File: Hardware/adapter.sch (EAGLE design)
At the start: 8 parts

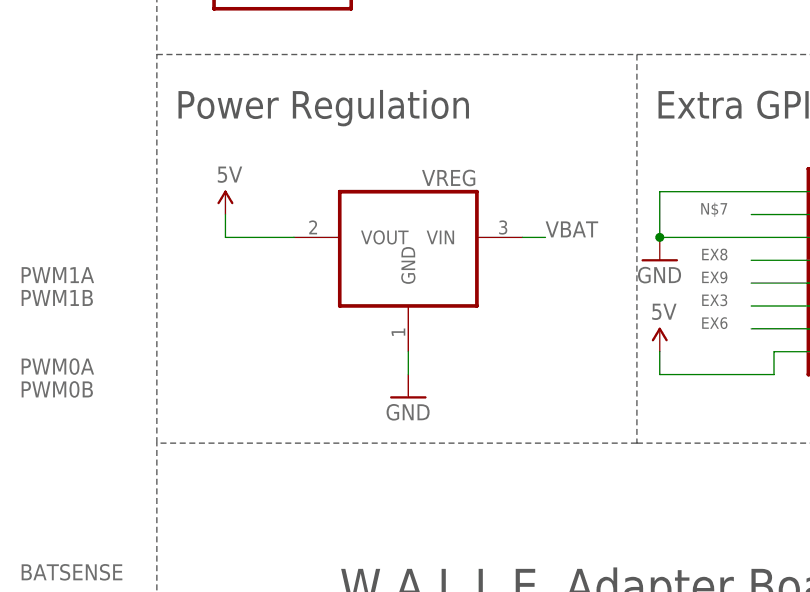
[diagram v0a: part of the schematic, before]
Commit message: Converted to TI LDO component.
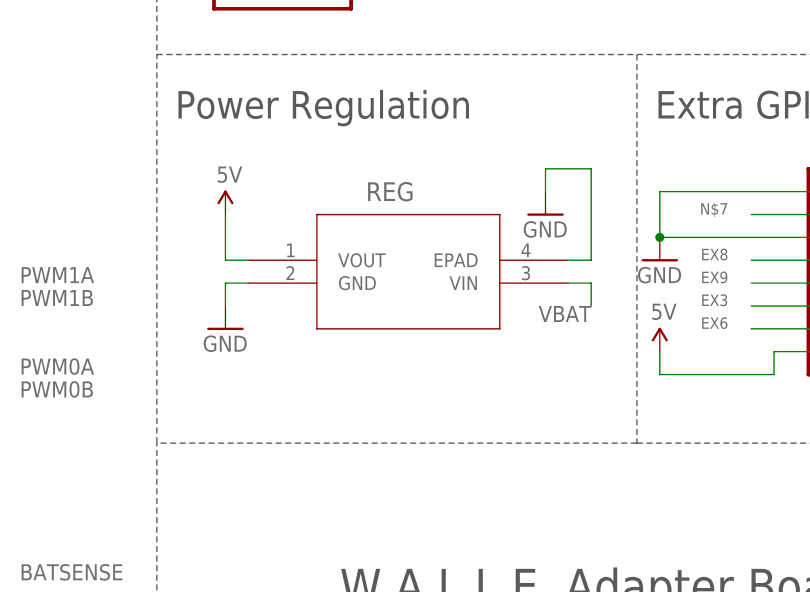
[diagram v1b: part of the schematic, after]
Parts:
- removed VREG: REG1117, burr-brown:REG1117
- added REG: UCC383-5_KTT_3, TI_UCC:UCC383-5_KTT_3
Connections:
- net 5V: now also REG.VOUT; no longer VREG.VOUT
- net GND: now also REG.EPAD, REG.GND; no longer VREG.GND
- net VBAT: now also REG.VIN; no longer VREG.VIN
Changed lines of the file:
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@@
 <part name="J1" library="pinhead" deviceset="PINHD-2X8" device=""/>
 <part name="J9" library="pinhead" deviceset="PINHD-2X8" device=""/>
-<part name="VREG" library="burr-brown" deviceset="REG1117" device=""/>
 <part name="GND9" library="supply1" deviceset="GND" device=""/>
 <part name="SUPPLY2" library="SparkFun-Aesthetics" deviceset="5V" device=""/>
@@
 <part name="GND11" library="supply1" deviceset="GND" device=""/>
 <part name="SUPPLY8" library="SparkFun-Aesthetics" deviceset="5V" device=""/>
+<part name="REG" library="TI_UCC" deviceset="UCC383-5_KTT_3" device=""/>
+<part name="GND12" library="supply1" deviceset="GND" device=""/>
 </parts>
 <sheets>
@@
 <attribute name="VALUE" x="146.05" y="93.98" size="1.778" layer="96" rot="MR180"/>
 </instance>
-<instance part="VREG" gate="G$1" x="111.76" y="38.1" smashed="yes" rot="MR0">
-<attribute name="NAME" x="119.38" y="43.815" size="1.778" layer="95" ratio="10" rot="MR0"/>
-</instance>
-<instance part="GND9" gate="1" x="111.76" y="20.32"/>
+<instance part="GND9" gate="1" x="91.44" y="27.94"/>
 <instance part="SUPPLY2" gate="G$1" x="-22.86" y="48.26"/>
 <instance part="SUPPLY3" gate="G$1" x="58.42" y="48.26"/>
@@
 <instance part="GND11" gate="1" x="177.8" y="20.32"/>
 <instance part="SUPPLY8" gate="G$1" x="139.7" y="25.4"/>
+<instance part="REG" gate="A" x="93.98" y="35.56" smashed="yes">
+<attribute name="NAME" x="107.0356" y="42.1386" size="2.0828" layer="95" ratio="6" rot="SR0"/>
+</instance>
+<instance part="GND12" gate="1" x="127" y="40.64"/>
 </instances>
 <busses>
@@
 <segment>
 <pinref part="GND9" gate="1" pin="GND"/>
-<pinref part="VREG" gate="G$1" pin="GND"/>
-<wire x1="111.76" y1="22.86" x2="111.76" y2="25.4" width="0.1524" layer="91"/>
+<wire x1="91.44" y1="30.48" x2="91.44" y2="33.02" width="0.1524" layer="91"/>
+<pinref part="REG" gate="A" pin="GND"/>
+<wire x1="91.44" y1="33.02" x2="93.98" y2="33.02" width="0.1524" layer="91"/>
 </segment>
 <segment>
@@
 <pinref part="GND11" gate="1" pin="GND"/>
 </segment>
+<segment>
+<pinref part="REG" gate="A" pin="EPAD"/>
+<wire x1="129.54" y1="35.56" x2="132.08" y2="35.56" width="0.1524" layer="91"/>
+<wire x1="132.08" y1="35.56" x2="132.08" y2="45.72" width="0.1524" layer="91"/>
+<pinref part="GND12" gate="1" pin="GND"/>
+<wire x1="132.08" y1="45.72" x2="127" y2="45.72" width="0.1524" layer="91"/>
+<wire x1="127" y1="45.72" x2="127" y2="43.18" width="0.1524" layer="91"/>
+</segment>
 </net>
 <net name="I2C1_SCL" class="0">
@@
 <net name="VBAT" class="0">
 <segment>
-<pinref part="VREG" gate="G$1" pin="VIN"/>
-<wire x1="124.46" y1="38.1" x2="127" y2="38.1" width="0.1524" layer="91"/>
-<label x="127" y="38.1" size="1.778" layer="95"/>
+<wire x1="129.54" y1="33.02" x2="132.08" y2="33.02" width="0.1524" layer="91"/>
+<label x="132.08" y="30.48" size="1.778" layer="95" rot="R180"/>
+<wire x1="132.08" y1="33.02" x2="132.08" y2="30.48" width="0.1524" layer="91"/>
+<pinref part="REG" gate="A" pin="VIN"/>
 </segment>
 <segment>
@@
 <net name="5V" class="0">
 <segment>
-<pinref part="VREG" gate="G$1" pin="VOUT"/>
-<wire x1="99.06" y1="38.1" x2="91.44" y2="38.1" width="0.1524" layer="91"/>
-<wire x1="91.44" y1="38.1" x2="91.44" y2="40.64" width="0.1524" layer="91"/>
+<wire x1="91.44" y1="35.56" x2="91.44" y2="40.64" width="0.1524" layer="91"/>
 <pinref part="SUPPLY7" gate="G$1" pin="5V"/>
-</segment>
-<segment>
+<pinref part="REG" gate="A" pin="VOUT"/>
+<wire x1="93.98" y1="35.56" x2="91.44" y2="35.56" width="0.1524" layer="91"/>
+</segment>
+<segment>

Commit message: Renamed WALLE to AVX on PCB.
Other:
- note added: "A.V.X. Adapter Board"
- note removed: "W.A.L.L.E. Adapter Board"
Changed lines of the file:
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@@
 <text x="85.852" y="51.308" size="3.048" layer="97">Power Regulation</text>
 <text x="-47.244" y="127.254" size="3.048" layer="97">BeagleBone Black</text>
-<text x="104.14" y="-2.54" size="3.81" layer="97">W.A.L.L.E. Adapter Board</text>
+<text x="104.14" y="-2.54" size="3.81" layer="97">A.V.X. Adapter Board</text>
 <wire x1="-50.8" y1="40.64" x2="-25.4" y2="40.64" width="0.1524" layer="97" style="shortdash"/>
 <wire x1="-25.4" y1="40.64" x2="-25.4" y2="5.08" width="0.1524" layer="97" style="shortdash"/>

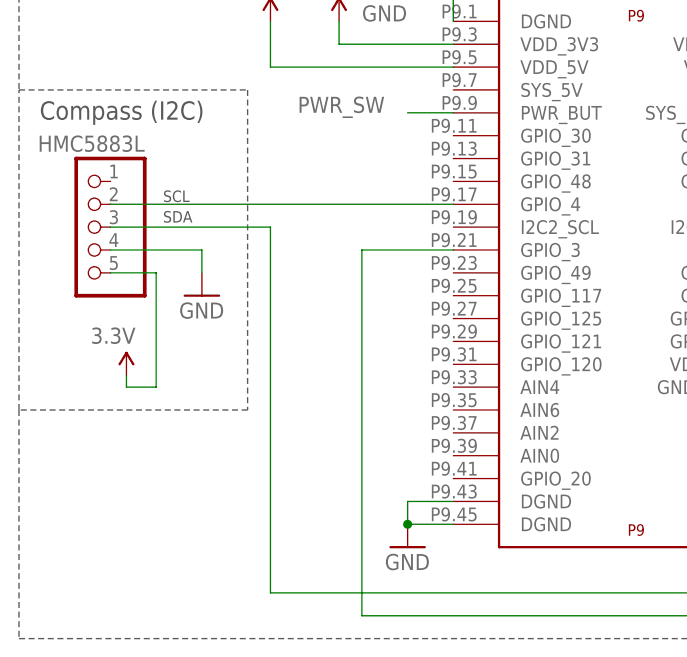
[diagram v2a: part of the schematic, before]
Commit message: Fixed issue with pinout for magnetometer. Updated layout ground plane vias.
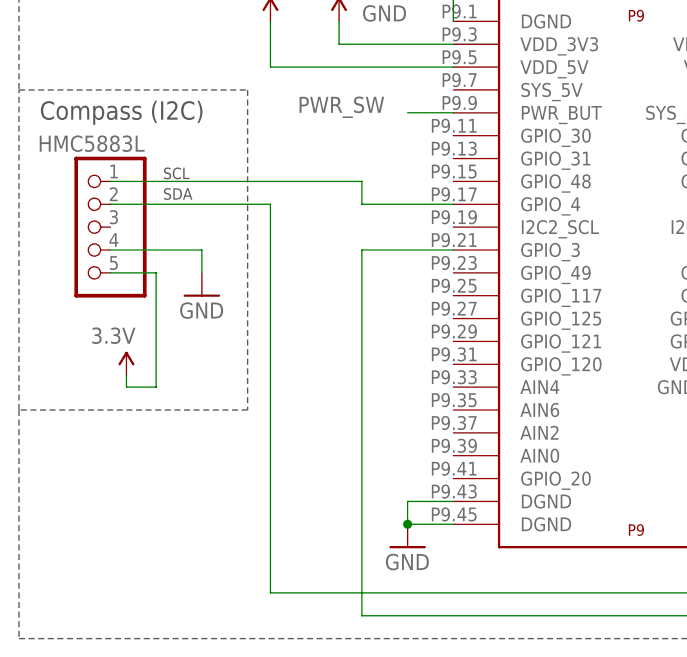
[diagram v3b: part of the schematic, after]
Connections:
- net I2C1_SCL: now also COMPASS.1; no longer COMPASS.2
- net I2C1_SDA: now also COMPASS.2; no longer COMPASS.3
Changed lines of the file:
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@@
 <wire x1="-50.8" y1="5.08" x2="-50.8" y2="40.64" width="0.1524" layer="97" style="shortdash"/>
 <text x="-48.514" y="37.338" size="2.032" layer="97">Compass (I2C)</text>
-<text x="-34.798" y="25.908" size="1.27" layer="97">SDA</text>
-<text x="-34.798" y="28.194" size="1.27" layer="97">SCL</text>
+<text x="-34.798" y="28.448" size="1.27" layer="97">SDA</text>
+<text x="-34.798" y="30.734" size="1.27" layer="97">SCL</text>
 <wire x1="137.16" y1="15.24" x2="187.96" y2="15.24" width="0.1524" layer="97" style="shortdash"/>
 <wire x1="187.96" y1="15.24" x2="187.96" y2="58.42" width="0.1524" layer="97" style="shortdash"/>
@@
 <net name="I2C1_SCL" class="0">
 <segment>
-<pinref part="COMPASS" gate="A" pin="2"/>
 <pinref part="U$1" gate="P9" pin="GPIO_4"/>
-<wire x1="-40.64" y1="27.94" x2="-2.54" y2="27.94" width="0.1524" layer="91"/>
+<pinref part="COMPASS" gate="A" pin="1"/>
+<wire x1="-12.7" y1="27.94" x2="-2.54" y2="27.94" width="0.1524" layer="91"/>
+<wire x1="-40.64" y1="30.48" x2="-12.7" y2="30.48" width="0.1524" layer="91"/>
+<wire x1="-12.7" y1="30.48" x2="-12.7" y2="27.94" width="0.1524" layer="91"/>
 </segment>
 </net>
@@
 <net name="I2C1_SDA" class="0">
 <segment>
-<pinref part="COMPASS" gate="A" pin="3"/>
-<wire x1="-40.64" y1="25.4" x2="-22.86" y2="25.4" width="0.1524" layer="91"/>
-<wire x1="-22.86" y1="25.4" x2="-22.86" y2="-15.24" width="0.1524" layer="91"/>
+<wire x1="-22.86" y1="27.94" x2="-22.86" y2="-15.24" width="0.1524" layer="91"/>
 <wire x1="-22.86" y1="-15.24" x2="48.26" y2="-15.24" width="0.1524" layer="91"/>
 <wire x1="48.26" y1="-15.24" x2="48.26" y2="27.94" width="0.1524" layer="91"/>
 <pinref part="U$1" gate="P9" pin="GPIO_5"/>
 <wire x1="48.26" y1="27.94" x2="38.1" y2="27.94" width="0.1524" layer="91"/>
-</segment>
-</net>
+<pinref part="COMPASS" gate="A" pin="2"/>
+<wire x1="-40.64" y1="27.94" x2="-22.86" y2="27.94" width="0.1524" layer="91"/>
+</segment>
+</net>
